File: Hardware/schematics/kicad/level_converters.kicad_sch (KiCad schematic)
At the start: 75 parts, among them U18 LM2902, U19 LM2902, U20 LM2902, U21 LM2902, U22 LM2902, U23 LM2902, U24 LM2902, U25 LM2902, U26 LM2902

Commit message: Modify schematics to suit a complete Eurorack PCB design
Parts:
- removed R97, R98: 220k, PCM_Resistor_SMD_AKL:R_0805_2012Metric_Pad1.15x1.40mm_HandSolder, symbol Device:R
- added J10: Osc CV Out 2, Connector_JST:JST_XH_B9B-XH-A_1x09_P2.50mm_Vertical, symbol Connector:Conn_01x09_Pin
- added J11: Velocity CV Out, Connector_JST:JST_XH_B9B-XH-A_1x09_P2.50mm_Vertical, symbol Connector:Conn_01x09_Pin
- added J12: Filter CV Out, Connector_JST:JST_XH_B9B-XH-A_1x09_P2.50mm_Vertical, symbol Connector:Conn_01x09_Pin
- added J13: Bend/Mod CV Out, Connector_JST:JST_XH_B4B-XH-A_1x04_P2.50mm_Vertical, symbol Connector:Conn_01x04_Pin
- added J9: Osc CV Out 1, Connector_JST:JST_XH_B9B-XH-A_1x09_P2.50mm_Vertical, symbol Connector:Conn_01x09_Pin
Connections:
- net GND: now also J10.9 (Pin_9), J11.9 (Pin_9), J12.9 (Pin_9), J13.4 (Pin_4), J9.9 (Pin_9)
- net 2V_POTS: no longer names the net of U26.13 (-)
- net 2V_POTS: no longer U26.14
- net BEND_CV: no longer names the net of U26.1, U26.2 (-)
- net BEND_CV: now also J13.1 (Pin_1)
- net CV1: no longer names the net of R34.1, U18.1
- net CV1: now also J9.1 (Pin_1)
- net CV10: no longer names the net of R52.1, U20.7
- net CV10: now also J10.2 (Pin_2)
- net CV11: no longer names the net of R54.1, U20.8
- net CV11: now also J10.3 (Pin_3)
- net CV12: no longer names the net of R56.1, U20.14
- net CV12: now also J10.4 (Pin_4)
- net CV13: no longer names the net of R58.1, U21.1
- net CV13: now also J10.5 (Pin_5)
- net CV14: no longer names the net of R60.1, U21.7
- net CV14: now also J10.6 (Pin_6)
- net CV15: no longer names the net of R62.1, U21.8
- net CV15: now also J10.7 (Pin_7)
- net CV16: no longer names the net of R64.1, U21.14
- net CV16: now also J10.8 (Pin_8)
- net CV2: no longer names the net of R36.1, U18.7
- net CV2: now also J9.2 (Pin_2)
- net CV3: no longer names the net of R38.1, U18.8
- net CV3: now also J9.3 (Pin_3)
- net CV4: no longer names the net of R40.1, U18.14
- net CV4: now also J9.4 (Pin_4)
- net CV5: no longer names the net of R42.1, U19.1
- net CV5: now also J9.5 (Pin_5)
- net CV6: no longer names the net of R44.1, U19.7
- net CV6: now also J9.6 (Pin_6)
- net CV7: no longer names the net of R46.1, U19.8
- net CV7: now also J9.7 (Pin_7)
- net CV8: no longer names the net of R48.1, U19.14
- net CV8: now also J9.8 (Pin_8)
- net CV9: no longer names the net of R50.1, U20.1
- net CV9: now also J10.1 (Pin_1)
- net FCV1: no longer names the net of R80.1, U24.1
- net FCV1: now also J12.1 (Pin_1)
- net FCV2: no longer names the net of R78.1, U24.7
- net FCV2: now also J12.2 (Pin_2)
- net FCV3: no longer names the net of R76.1, U24.8
- net FCV3: now also J12.3 (Pin_3)
- net FCV4: no longer names the net of R74.1, U24.14
- net FCV4: now also J12.4 (Pin_4)
- net FCV5: no longer names the net of R72.1, U25.1
- net FCV5: now also J12.5 (Pin_5)
- net FCV6: no longer names the net of R70.1, U25.7
- net FCV6: now also J12.6 (Pin_6)
- net FCV7: no longer names the net of R68.1, U25.8
- net FCV7: now also J12.7 (Pin_7)
- net FCV8: no longer names the net of R66.1, U25.14
- net FCV8: now also J12.8 (Pin_8)
- net MOD2_CV: no longer names the net of U26.8, U26.9 (-)
- net MOD2_CV: now also J13.3 (Pin_3)
- net MOD_CV: no longer names the net of U26.6 (-), U26.7
- net MOD_CV: now also J13.2 (Pin_2)
- net VELOCITY_CV1: no longer names the net of R82.1, U22.1
- net VELOCITY_CV1: now also J11.1 (Pin_1)
- net VELOCITY_CV2: no longer names the net of R84.1, U22.7
- net VELOCITY_CV2: now also J11.2 (Pin_2)
- net VELOCITY_CV3: no longer names the net of R86.1, U22.8
- net VELOCITY_CV3: now also J11.3 (Pin_3)
- net VELOCITY_CV4: no longer names the net of R88.1, U22.14
- net VELOCITY_CV4: now also J11.4 (Pin_4)
- net VELOCITY_CV5: no longer names the net of R90.1, U23.1
- net VELOCITY_CV5: now also J11.5 (Pin_5)
- net VELOCITY_CV6: no longer names the net of R92.1, U23.7
- net VELOCITY_CV6: now also J11.6 (Pin_6)
- net VELOCITY_CV7: no longer names the net of R94.1, U23.8
- net VELOCITY_CV7: now also J11.7 (Pin_7)
- net VELOCITY_CV8: no longer names the net of R96.1, U23.14
- net VELOCITY_CV8: now also J11.8 (Pin_8)
- no-connect marks 0 -> 3
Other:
- note added: "Bend Mod"
- moved on the sheet: R33, R34, R35, R36, R37, R38, R39, R40, R41, R42, R43, R44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

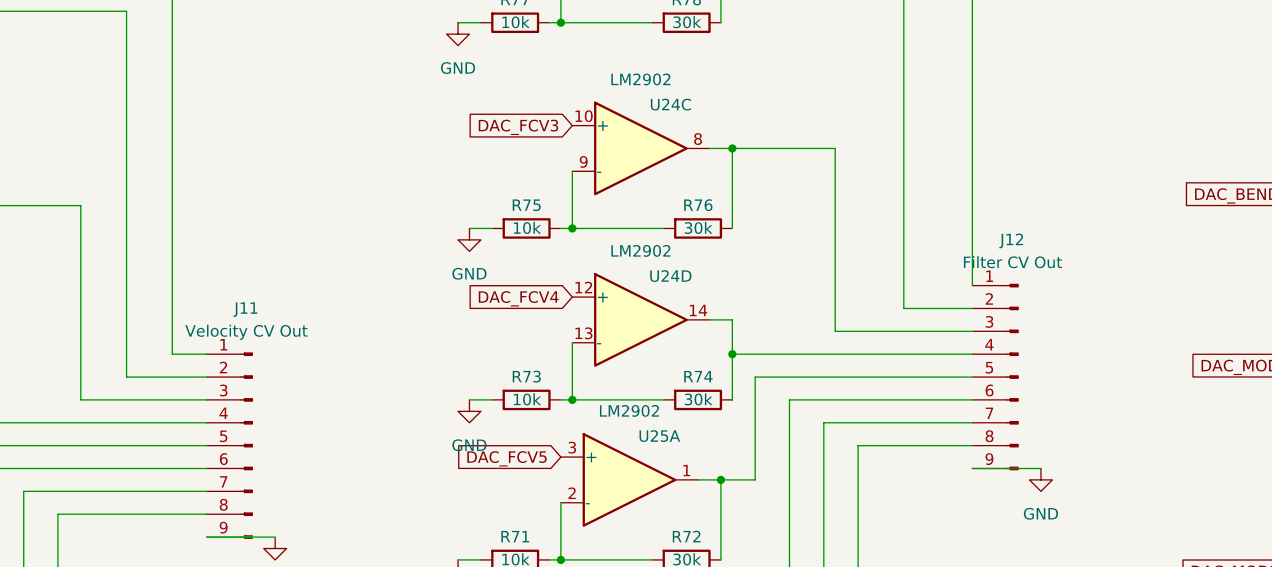
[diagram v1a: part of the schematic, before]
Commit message: Fix schematic bug
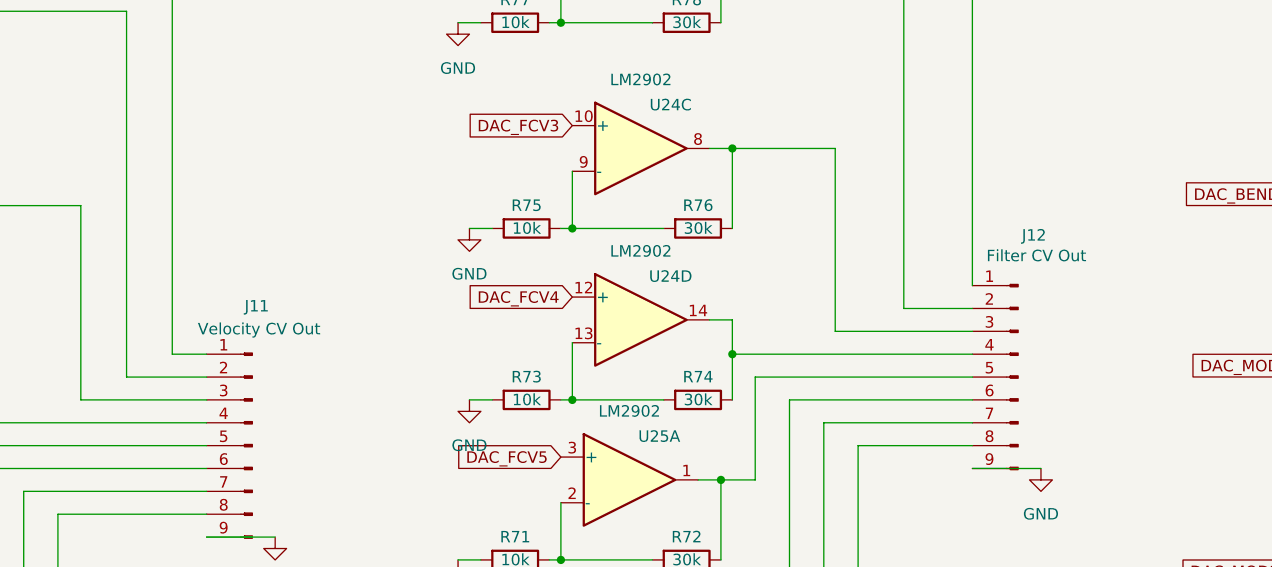
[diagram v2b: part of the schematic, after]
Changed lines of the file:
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@@
 		(dnp no)
 		(property "Reference" "J11"
-			(at 249.555 115.57 0)
+			(at 250.698 115.316 0)
 			(effects
 				(font
@@
 		)
 		(property "Value" "Velocity CV Out"
-			(at 249.555 118.11 0)
+			(at 250.952 117.856 0)
 			(effects
 				(font
@@
 		(dnp no)
 		(property "Reference" "J12"
-			(at 334.645 107.95 0)
+			(at 337.058 107.442 0)
 			(effects
 				(font
@@
 		)
 		(property "Value" "Filter CV Out"
-			(at 334.645 110.49 0)
-			(effects
-				(font
+			(at 337.312 109.728 0)
+			(effects
+				(font

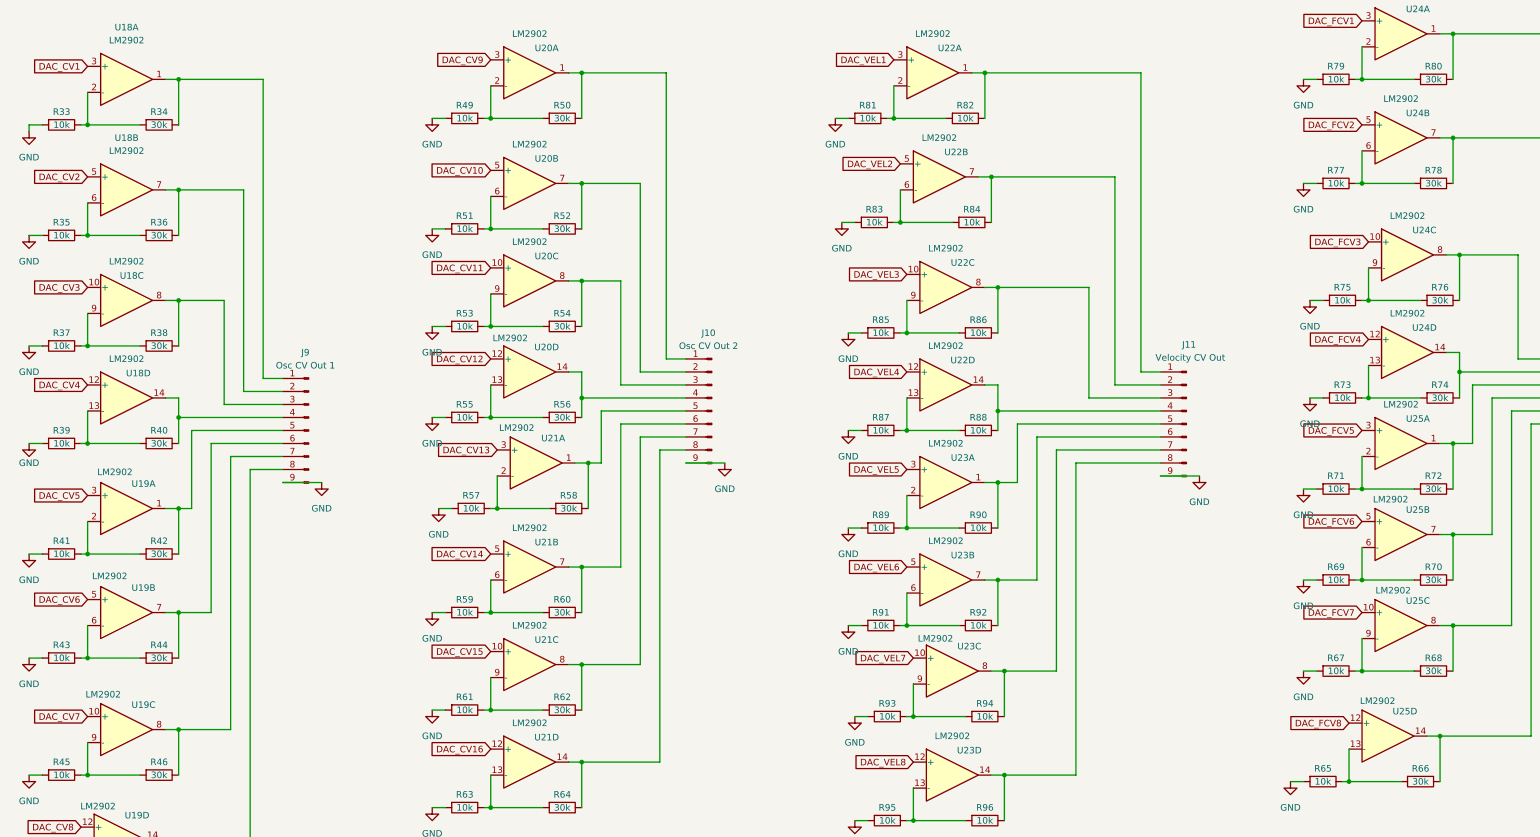
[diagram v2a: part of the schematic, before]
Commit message: Remove LFO in favor of standalone LFO and create PCB. FM Input still exists in case it's needed.
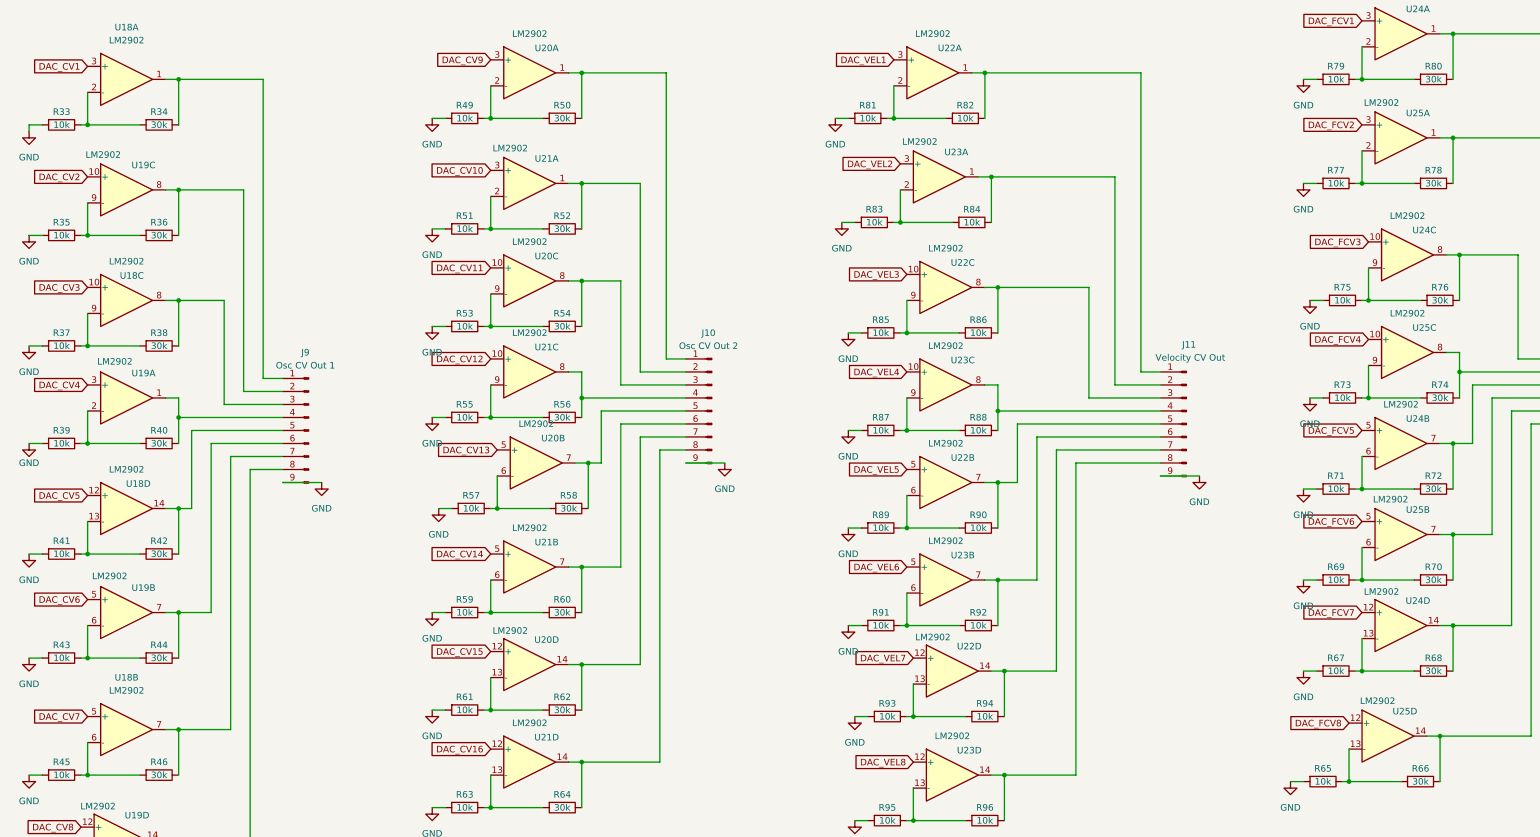
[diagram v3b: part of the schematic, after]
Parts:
- J10, J11, J9: footprint Connector_JST:JST_XH_B9B-XH-A_1x09_P2.50mm_Vertical -> Connector_IDC:IDC-Header_2x05_P2.54mm_Vertical
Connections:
- net DAC_CV10: now also U21.3 (+); no longer U20.5 (+)
- net DAC_CV12: now also U21.10 (+); no longer U20.12 (+)
- net DAC_CV13: now also U20.5 (+); no longer U21.3 (+)
- net DAC_CV15: now also U20.12 (+); no longer U21.10 (+)
- net DAC_CV2: now also U19.10 (+); no longer U18.5 (+)
- net DAC_CV4: now also U19.3 (+); no longer U18.12 (+)
- net DAC_CV5: now also U18.12 (+); no longer U19.3 (+)
- net DAC_CV7: now also U18.5 (+); no longer U19.10 (+)
- net DAC_FCV2: now also U25.3 (+); no longer U24.5 (+)
- net DAC_FCV4: now also U25.10 (+); no longer U24.12 (+)
- net DAC_FCV5: now also U24.5 (+); no longer U25.3 (+)
- net DAC_FCV7: now also U24.12 (+); no longer U25.10 (+)
- net DAC_VEL2: now also U23.3 (+); no longer U22.5 (+)
- net DAC_VEL4: now also U23.10 (+); no longer U22.12 (+)
- net DAC_VEL5: now also U22.5 (+); no longer U23.3 (+)
- net DAC_VEL7: now also U22.12 (+); no longer U23.10 (+)
- net at J10.7 (Pin_7), R62.1: now also U20.14; no longer U21.8
- net at R61.1, R62.2: now also U20.13 (-); no longer U21.9 (-)
- net at J9.7 (Pin_7), R46.1: now also U18.7; no longer U19.8
- net at R45.1, R46.2: now also U18.6 (-); no longer U19.9 (-)
- net at R73.1, R74.2: now also U25.9 (-); no longer U24.13 (-)
- net at J12.4 (Pin_4), R74.1: now also U25.8; no longer U24.14
- net at J11.5 (Pin_5), R90.1: now also U22.7; no longer U23.1
- net at R89.1, R90.2: now also U22.6 (-); no longer U23.2 (-)
- net at R87.1, R88.2: now also U23.9 (-); no longer U22.13 (-)
- net at R55.1, R56.2: now also U21.9 (-); no longer U20.13 (-)
- net at J11.7 (Pin_7), R94.1: now also U22.14; no longer U23.8
- net at R93.1, R94.2: now also U22.13 (-); no longer U23.9 (-)
- net at R51.1, R52.2: now also U21.2 (-); no longer U20.6 (-)
- net at J10.2 (Pin_2), R52.1: now also U21.1; no longer U20.7
- net at J10.5 (Pin_5), R58.1: now also U20.7; no longer U21.1
- net at R57.1, R58.2: now also U20.6 (-); no longer U21.2 (-)
- net at J11.2 (Pin_2), R84.1: now also U23.1; no longer U22.7
- net at J11.4 (Pin_4), R88.1: now also U23.8; no longer U22.14
- net at J9.2 (Pin_2), R36.1: now also U19.8; no longer U18.7
- net at J9.4 (Pin_4), R40.1: now also U19.1; no longer U18.14
- net at J9.5 (Pin_5), R42.1: now also U18.14; no longer U19.1
- net at J10.4 (Pin_4), R56.1: now also U21.8; no longer U20.14
- net at R77.1, R78.2: now also U25.2 (-); no longer U24.6 (-)
- net at J12.2 (Pin_2), R78.1: now also U25.1; no longer U24.7
- net at R41.1, R42.2: now also U18.13 (-); no longer U19.2 (-)
- net at R67.1, R68.2: now also U24.13 (-); no longer U25.9 (-)
- net at J12.5 (Pin_5), R72.1: now also U24.7; no longer U25.1
- net at J12.7 (Pin_7), R68.1: now also U24.14; no longer U25.8
- net at R39.1, R40.2: now also U19.2 (-); no longer U18.13 (-)
- net at R83.1, R84.2: now also U23.2 (-); no longer U22.6 (-)
- net at R35.1, R36.2: now also U19.9 (-); no longer U18.6 (-)
- net at R71.1, R72.2: now also U24.6 (-); no longer U25.2 (-)
